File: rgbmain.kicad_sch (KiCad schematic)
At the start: 14 parts, among them J1 Conn_01x10_Pin, J10 Conn_01x04, J2 Conn_01x10_Pin, J3 Conn_01x09_Pin, J4 Conn_01x09, J5 Conn_01x06_Pin, J6 Conn_01x06, J7 Conn_01x13, J8 Conn_01x13, J9 Conn_01x01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

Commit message: footprints added
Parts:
- J1, J2: footprint (none) -> Connector_Molex:Molex_KK-396_A-41792-0010_1x10_P3.96mm_Horizontal
- J10: footprint (none) -> Connector_PinSocket_2.54mm:PinSocket_1x04_P2.54mm_Vertical
- J3, J4: footprint (none) -> Connector_Molex:Molex_KK-396_A-41792-0009_1x09_P3.96mm_Horizontal
- J5, J6: footprint (none) -> Connector_Molex:Molex_KK-396_A-41792-0006_1x06_P3.96mm_Horizontal
- J7, J8: footprint (none) -> rgbmain:Molex_0039532135
- J9: footprint (none) -> Connector_PinHeader_1.00mm:PinHeader_1x01_P1.00mm_Vertical
- R1, R2: footprint (none) -> Resistor_SMD:R_0805_2012Metric_Pad1.20x1.40mm_HandSolder
- U1: footprint (none) -> rgbmain:ElitePi
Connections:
- net +3V3: now also J10.2 (Pin_2); no longer J10.3 (Pin_3)
- net GND: now also J10.1 (Pin_1); no longer J10.4 (Pin_4)
- net SDA0: now also J10.3 (Pin_3); no longer J10.2 (Pin_2)
- net SLC0: now also J10.4 (Pin_4); no longer J10.1 (Pin_1)
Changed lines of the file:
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@@
+	(wire
+		(pts
+			(xy 102.87 26.67) (xy 118.11 26.67)
+		)
+		(stroke
+			(width 0)
+			(type default)
+		)
+	)
 	(wire
 		(pts
@@
 		(pts
 			(xy 121.92 109.22) (xy 121.92 111.76)
-		)
-		(stroke
-			(width 0)
-			(type default)
-		)
-	)
-	(wire
-		(pts
-			(xy 113.03 26.67) (xy 118.11 26.67)
 		)
 		(stroke
@@
 		)
 	)
+	(label "SDA0"
+		(at 113.03 31.75 180)
+		(effects
+			(font
+				(size 1.27 1.27)
+			)
+			(justify right bottom)
+		)
+	)
 	(label "COL_4"
 		(at 30.48 74.93 180)
@@
 		)
 	)
-	(label "SLC0"
-		(at 113.03 26.67 180)
-		(effects
-			(font
-				(size 1.27 1.27)
-			)
-			(justify right bottom)
-		)
-	)
 	(label "ROW_6"
 		(at 162.56 77.47 0)
@@
 		)
 	)
-	(label "SDA0"
-		(at 113.03 29.21 180)
-		(effects
-			(font
-				(size 1.27 1.27)
-			)
-			(justify right bottom)
-		)
-	)
 	(label "COL_9"
 		(at 246.38 72.39 0)
@@
 		)
 	)
+	(label "SLC0"
+		(at 113.03 34.29 180)
+		(effects
+			(font
+				(size 1.27 1.27)
+			)
+			(justify right bottom)
+		)
+	)
 	(label "DOUT_KEY_3V3"
 		(at 162.56 64.77 0)
@@
 			)
 			(justify right bottom)
+		)
+	)
+	(symbol
+		(lib_id "power:+3V3")
+		(at 113.03 29.21 90)
+		(unit 1)
+		(exclude_from_sim no)
+		(in_bom yes)
+		(on_board yes)
+		(dnp no)
+		(fields_autoplaced yes)
+		(property "Reference" "#PWR07"
+			(at 116.84 29.21 0)
+			(effects
+				(font
+					(size 1.27 1.27)
+				)
+				(hide yes)
+			)
+		)
+		(property "Value" "+3V3"
+			(at 109.22 29.2099 90)
+			(effects
+				(font
+					(size 1.27 1.27)
+				)
+				(justify left)
+			)
+		)
+		(property "Footprint" ""
+			(at 113.03 29.21 0)
+			(effects
+				(font
+					(size 1.27 1.27)
+				)
+				(hide yes)
+			)
+		)
+		(property "Datasheet" ""
+			(at 113.03 29.21 0)
+			(effects
+				(font
+					(size 1.27 1.27)
+				)
+				(hide yes)
+			)
+		)
+		(property "Description" "Power symbol creates a global label with name \"+3V3\""
+			(at 113.03 29.21 0)
+			(effects
+				(font
+					(size 1.27 1.27)
+				)
+				(hide yes)
+			)
+		)
+		(pin "1"
+		)
+		(instances
+			(project ""
+				(path "/24ca604d-a7a4-46c7-a288-45b7cfc45cc9"
+					(reference "#PWR07")
+					(unit 1)
+				)
+			)
 		)
 	)
@@
 			)
 		)
-		(property "Footprint" ""
+		(property "Footprint" "rgbmain:Molex_0039532135"
 			(at 38.1 40.64 0)
 			(effects
@@
 			)
 		)
-		(property "Footprint" ""
+		(property "Footprint" "Connector_Molex:Molex_KK-396_A-41792-0006_1x06_P3.96mm_Horizontal"
 			(at 238.76 72.39 0)
 			(effects
@@
 			)
 		)
-		(property "Footprint" ""
+		(property "Footprint" "Connector_Molex:Molex_KK-396_A-41792-0010_1x10_P3.96mm_Horizontal"
 			(at 161.29 144.78 0)
 			(effects
@@
 			)
 		)
-		(property "Footprint" ""
+		(property "Footprint" "Resistor_SMD:R_0805_2012Metric_Pad1.20x1.40mm_HandSolder"
 			(at 187.452 30.48 90)
 			(effects
@@
 			)
 		)
-		(property "Footprint" ""
+		(property "Footprint" "Connector_Molex:Molex_KK-396_A-41792-0006_1x06_P3.96mm_Horizontal"
 			(at 38.1 72.39 0)
 			(effects
@@
 			)
 		)
-		(property "Footprint" ""
+		(property "Footprint" "Connector_Molex:Molex_KK-396_A-41792-0010_1x10_P3.96mm_Horizontal"
 			(at 127 144.78 0)
 			(effects
@@
 				(path "/24ca604d-a7a4-46c7-a288-45b7cfc45cc9"
 					(reference "J1")
+					(unit 1)
+				)
+			)
+		)
+	)
+	(symbol
+		(lib_id "power:GND")
+		(at 102.87 26.67 0)
+		(unit 1)
+		(exclude_from_sim no)
+		(in_bom yes)
+		(on_board yes)
+		(dnp no)
+		(fields_autoplaced yes)
+		(property "Reference" "#PWR06"
+			(at 102.87 33.02 0)
+			(effects
+				(font
+					(size 1.27 1.27)
+				)
+				(hide yes)
+			)
+		)
+		(property "Value" "GND"
+			(at 102.87 31.75 0)
+			(effects
+				(font
+					(size 1.27 1.27)
+				)
+			)
+		)
+		(property "Footprint" ""
+			(at 102.87 26.67 0)
+			(effects
+				(font
+					(size 1.27 1.27)
+				)
+				(hide yes)
+			)
+		)
+		(property "Datasheet" ""
+			(at 102.87 26.67 0)
+			(effects
+				(font
+					(size 1.27 1.27)
+				)
+				(hide yes)
+			)
+		)
+		(property "Description" "Power symbol creates a global label with name \"GND\" , ground"
+			(at 102.87 26.67 0)
+			(effects
+				(font
+					(size 1.27 1.27)
+				)
+				(hide yes)
+			)
+		)
+		(pin "1"
+		)
+		(instances
+			(project ""
+				(path "/24ca604d-a7a4-46c7-a288-45b7cfc45cc9"
+					(reference "#PWR06")
 					(unit 1)
 				)
@@
 			)
 		)
-		(property "Footprint" ""
+		(property "Footprint" "Resistor_SMD:R_0805_2012Metric_Pad1.20x1.40mm_HandSolder"
 			(at 200.152 30.48 90)
 			(effects
@@
 	)
 	(symbol
-		(lib_id "power:+3V3")
-		(at 113.03 31.75 90)
-		(unit 1)
-		(exclude_from_sim no)
-		(in_bom yes)
-		(on_board yes)
-		(dnp no)
-		(fields_autoplaced yes)
-		(property "Reference" "#PWR07"
-			(at 116.84 31.75 0)
-			(effects
-				(font
-					(size 1.27 1.27)
-				)
-				(hide yes)
-			)
-		)
-		(property "Value" "+3V3"
-			(at 109.22 31.7499 90)
-			(effects
-				(font
-					(size 1.27 1.27)
-				)
-				(justify left)
-			)
-		)
-		(property "Footprint" ""
-			(at 113.03 31.75 0)
-			(effects
-				(font
-					(size 1.27 1.27)
-				)
-				(hide yes)
-			)
-		)
-		(property "Datasheet" ""
-			(at 113.03 31.75 0)
-			(effects
-				(font
-					(size 1.27 1.27)
-				)
-				(hide yes)
-			)
-		)
-		(property "Description" "Power symbol creates a global label with name \"+3V3\""
-			(at 113.03 31.75 0)
-			(effects
-				(font
-					(size 1.27 1.27)
-				)
-				(hide yes)
-			)
-		)
-		(pin "1"
-		)
-		(instances
-			(project ""
-				(path "/24ca604d-a7a4-46c7-a288-45b7cfc45cc9"
-					(reference "#PWR07")
-					(unit 1)
-				)
-			)
-		)
-	)
-	(symbol
 		(lib_id "Connector_Generic:Conn_01x01")
 		(at 129.54 104.14 0)
@@
 			)
 		)
-		(property "Footprint" ""
+		(property "Footprint" "Connector_PinHeader_1.00mm:PinHeader_1x01_P1.00mm_Vertical"
 			(at 129.54 104.14 0)
 			(effects
@@
 			)
 		)
-		(property "Footprint" ""
+		(property "Footprint" "rgbmain:ElitePi"
 			(at 144.78 62.23 0)
 			(effects
@@
 			)
 		)
-		(property "Footprint" ""
+		(property "Footprint" "Connector_Molex:Molex_KK-396_A-41792-0009_1x09_P3.96mm_Horizontal"
 			(at 238.76 105.41 0)
 			(effects
@@
 			)
 		)
-		(property "Footprint" ""
+		(property "Footprint" "Connector_Molex:Molex_KK-396_A-41792-0009_1x09_P3.96mm_Horizontal"
 			(at 38.1 105.41 0)
 			(effects
@@
 			)
 		)
-		(property "Footprint" ""
+		(property "Footprint" "Connector_PinSocket_2.54mm:PinSocket_1x04_P2.54mm_Vertical"
 			(at 123.19 29.21 0)
 			(effects
@@
 			)
 		)
-		(property "Footprint" ""
+		(property "Footprint" "rgbmain:Molex_0039532135"
 			(at 238.76 40.64 0)
 			(effects
@@
 					(unit 1)
 				)
-			)
-		)
-	)
-	(symbol
-		(lib_id "power:GND")
-		(at 113.03 34.29 0)
-		(unit 1)
-		(exclude_from_sim no)
-		(in_bom yes)
-		(on_board yes)
-		(dnp no)
-		(fields_autoplaced yes)
-		(property "Reference" "#PWR06"
-			(at 113.03 40.64 0)
-			(effects
-				(font
-					(size 1.27 1.27)
-				)
-				(hide yes)
-			)
-		)
-		(property "Value" "GND"
-			(at 113.03 39.37 0)
-			(effects
-				(font
-					(size 1.27 1.27)
-				)
-			)
-		)
-		(property "Footprint" ""
-			(at 113.03 34.29 0)
-			(effects
-				(font
-					(size 1.27 1.27)
-				)
-				(hide yes)
-			)
-		)
-		(property "Datasheet" ""
-			(at 113.03 34.29 0)
-			(effects
-				(font
-					(size 1.27 1.27)
-				)
-				(hide yes)
-			)
-		)
-		(property "Description" "Power symbol creates a global label with name \"GND\" , ground"
-			(at 113.03 34.29 0)
-			(effects
-				(font
-					(size 1.27 1.27)
-				)
-				(hide yes)
-			)
-		)
-		(pin "1"
-		)
-		(instances
-			(project ""
-				(path "/24ca604d-a7a4-46c7-a288-45b7cfc45cc9"
-					(reference "#PWR06")
-					(unit 1)
-				)

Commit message: use the Molex KK *2.54*
footprints sourced from: https://github.com/SnowMB/pcb_library
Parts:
- added H1: mounting pad, MountingHole:MountingHole_4.3mm_M4_Pad, symbol Mechanical:MountingHole_Pad
- J1, J2: footprint Connector_Molex:Molex_KK-396_A-41792-0010_1x10_P3.96mm_Horizontal -> rgbmain:Molex_KK-254_1x10_P2.54mm_Horizontal
- J3, J4: footprint Connector_Molex:Molex_KK-396_A-41792-0009_1x09_P3.96mm_Horizontal -> rgbmain:Molex_KK-254_1x09_P2.54mm_Horizontal
- J5, J6: footprint Connector_Molex:Molex_KK-396_A-41792-0006_1x06_P3.96mm_Horizontal -> rgbmain:Molex_KK-254_1x06_P2.54mm_Horizontal
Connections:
- net GND: now also H1.1
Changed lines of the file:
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@@
+	(wire
+		(pts
+			(xy 78.74 87.63) (xy 78.74 85.09)
+		)
+		(stroke
+			(width 0)
+			(type default)
+		)
+	)
 	(wire
 		(pts
@@
 		(pts
 			(xy 113.03 29.21) (xy 118.11 29.21)
+		)
+		(stroke
+			(width 0)
+			(type default)
+		)
+	)
+	(wire
+		(pts
+			(xy 78.74 85.09) (xy 88.9 85.09)
 		)
 		(stroke
@@
 				(path "/24ca604d-a7a4-46c7-a288-45b7cfc45cc9"
 					(reference "J7")
+					(unit 1)
+				)
+			)
+		)
+	)
+	(symbol
+		(lib_id "Mechanical:MountingHole_Pad")
+		(at 91.44 85.09 270)
+		(unit 1)
+		(exclude_from_sim no)
+		(in_bom yes)
+		(on_board yes)
+		(dnp no)
+		(property "Reference" "H1"
+			(at 92.0242 87.884 0)
+			(effects
+				(font
+					(size 1.4986 1.4986)
+				)
+				(justify left bottom)
+				(hide yes)
+			)
+		)
+		(property "Value" "mounting pad"
+			(at 83.82 88.9 90)
+			(effects
+				(font
+					(size 1.4986 1.4986)
+				)
+				(justify left bottom)
+			)
+		)
+		(property "Footprint" "MountingHole:MountingHole_4.3mm_M4_Pad"
+			(at 91.44 85.09 0)
+			(effects
+				(font
+					(size 1.27 1.27)
+				)
+				(hide yes)
+			)
+		)
+		(property "Datasheet" ""
+			(at 91.44 85.09 0)
+			(effects
+				(font
+					(size 1.27 1.27)
+				)
+				(hide yes)
+			)
+		)
+		(property "Description" ""
+			(at 91.44 85.09 0)
+			(effects
+				(font
+					(size 1.27 1.27)
+				)
+			)
+		)
+		(pin "1"
+		)
+		(instances
+			(project "rgbmain"
+				(path "/24ca604d-a7a4-46c7-a288-45b7cfc45cc9"
+					(reference "H1")
 					(unit 1)
 				)
@@
 			)
 		)
-		(property "Footprint" "Connector_Molex:Molex_KK-396_A-41792-0006_1x06_P3.96mm_Horizontal"
+		(property "Footprint" "rgbmain:Molex_KK-254_1x06_P2.54mm_Horizontal"
 			(at 238.76 72.39 0)
 			(effects
@@
 			)
 		)
-		(property "Footprint" "Connector_Molex:Molex_KK-396_A-41792-0010_1x10_P3.96mm_Horizontal"
+		(property "Footprint" "rgbmain:Molex_KK-254_1x10_P2.54mm_Horizontal"
 			(at 161.29 144.78 0)
 			(effects
@@
 			)
 		)
-		(property "Footprint" "Connector_Molex:Molex_KK-396_A-41792-0006_1x06_P3.96mm_Horizontal"
+		(property "Footprint" "rgbmain:Molex_KK-254_1x06_P2.54mm_Horizontal"
 			(at 38.1 72.39 0)
 			(effects
@@
 			)
 		)
-		(property "Footprint" "Connector_Molex:Molex_KK-396_A-41792-0010_1x10_P3.96mm_Horizontal"
+		(property "Footprint" "rgbmain:Molex_KK-254_1x10_P2.54mm_Horizontal"
 			(at 127 144.78 0)
 			(effects
@@
 			)
 		)
-		(property "Footprint" "Connector_Molex:Molex_KK-396_A-41792-0009_1x09_P3.96mm_Horizontal"
+		(property "Footprint" "rgbmain:Molex_KK-254_1x09_P2.54mm_Horizontal"
 			(at 238.76 105.41 0)
 			(effects
@@
 			)
 		)
-		(property "Footprint" "Connector_Molex:Molex_KK-396_A-41792-0009_1x09_P3.96mm_Horizontal"
+		(property "Footprint" "rgbmain:Molex_KK-254_1x09_P2.54mm_Horizontal"
 			(at 38.1 105.41 0)
 			(effects
@@
 					(unit 1)
 				)
+			)
+		)
+	)
+	(symbol
+		(lib_id "power:GND")
+		(at 78.74 87.63 0)
+		(unit 1)
+		(exclude_from_sim no)
+		(in_bom yes)
+		(on_board yes)
+		(dnp no)
+		(fields_autoplaced yes)
+		(property "Reference" "#PWR08"
+			(at 78.74 93.98 0)
+			(effects
+				(font
+					(size 1.27 1.27)
+				)
+				(hide yes)
+			)
+		)
+		(property "Value" "GND"
+			(at 78.74 92.71 0)
+			(effects
+				(font
+					(size 1.27 1.27)
+				)
+			)
+		)
+		(property "Footprint" ""
+			(at 78.74 87.63 0)
+			(effects
+				(font
+					(size 1.27 1.27)
+				)
+				(hide yes)
+			)
+		)
+		(property "Datasheet" ""
+			(at 78.74 87.63 0)
+			(effects
+				(font
+					(size 1.27 1.27)
+				)
+				(hide yes)
+			)
+		)
+		(property "Description" "Power symbol creates a global label with name \"GND\" , ground"
+			(at 78.74 87.63 0)
+			(effects
+				(font
+					(size 1.27 1.27)
+				)
+				(hide yes)
+			)
+		)
+		(pin "1"
+		)
+		(instances
+			(project ""
+				(path "/24ca604d-a7a4-46c7-a288-45b7cfc45cc9"
+					(reference "#PWR08")
+					(unit 1)
+				)

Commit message: use vertical pcb connectors
horizontal take up too much board space
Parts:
- J1, J2: footprint rgbmain:Molex_KK-254_1x10_P2.54mm_Horizontal -> Connector_Molex:Molex_KK-254_AE-6410-10A_1x10_P2.54mm_Vertical
- J3, J4: footprint rgbmain:Molex_KK-254_1x09_P2.54mm_Horizontal -> Connector_Molex:Molex_KK-254_AE-6410-09A_1x09_P2.54mm_Vertical
- J5, J6: footprint rgbmain:Molex_KK-254_1x06_P2.54mm_Horizontal -> Connector_Molex:Molex_KK-254_AE-6410-06A_1x06_P2.54mm_Vertical
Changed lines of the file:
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@@
 			)
 		)
-		(property "Footprint" "rgbmain:Molex_KK-254_1x06_P2.54mm_Horizontal"
+		(property "Footprint" "Connector_Molex:Molex_KK-254_AE-6410-06A_1x06_P2.54mm_Vertical"
 			(at 238.76 72.39 0)
 			(effects
@@
 			)
 		)
-		(property "Footprint" "rgbmain:Molex_KK-254_1x10_P2.54mm_Horizontal"
+		(property "Footprint" "Connector_Molex:Molex_KK-254_AE-6410-10A_1x10_P2.54mm_Vertical"
 			(at 161.29 144.78 0)
 			(effects
@@
 			)
 		)
-		(property "Footprint" "rgbmain:Molex_KK-254_1x06_P2.54mm_Horizontal"
+		(property "Footprint" "Connector_Molex:Molex_KK-254_AE-6410-06A_1x06_P2.54mm_Vertical"
 			(at 38.1 72.39 0)
 			(effects
@@
 			)
 		)
-		(property "Footprint" "rgbmain:Molex_KK-254_1x10_P2.54mm_Horizontal"
+		(property "Footprint" "Connector_Molex:Molex_KK-254_AE-6410-10A_1x10_P2.54mm_Vertical"
 			(at 127 144.78 0)
 			(effects
@@
 			)
 		)
-		(property "Footprint" "rgbmain:Molex_KK-254_1x09_P2.54mm_Horizontal"
+		(property "Footprint" "Connector_Molex:Molex_KK-254_AE-6410-09A_1x09_P2.54mm_Vertical"
 			(at 238.76 105.41 0)
 			(effects
@@
 			)
 		)
-		(property "Footprint" "rgbmain:Molex_KK-254_1x09_P2.54mm_Horizontal"
+		(property "Footprint" "Connector_Molex:Molex_KK-254_AE-6410-09A_1x09_P2.54mm_Vertical"
 			(at 38.1 105.41 0)
 			(effects

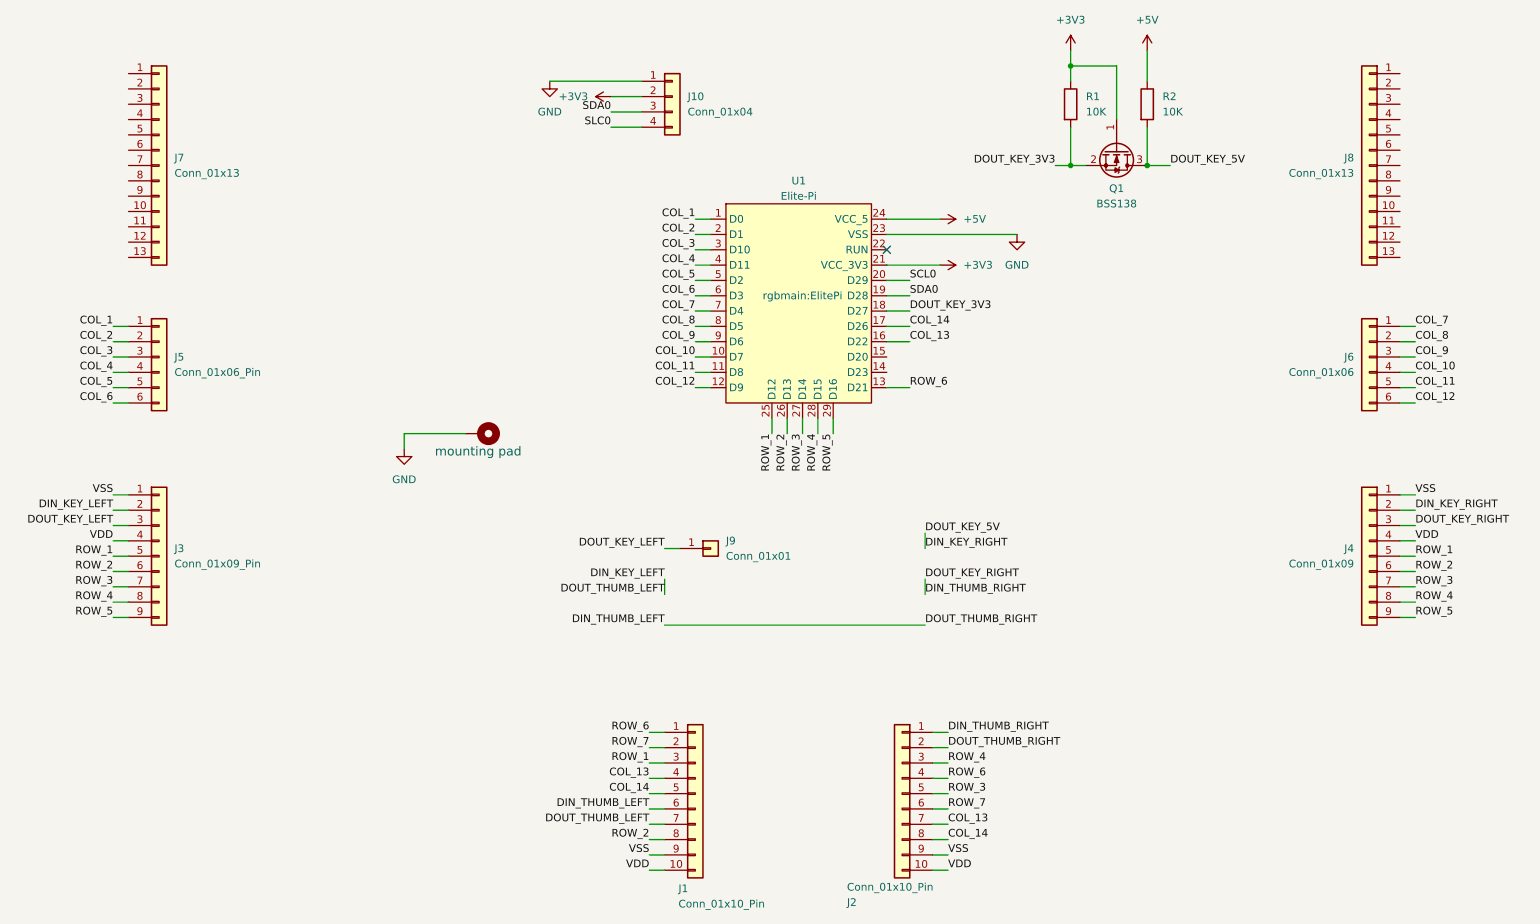
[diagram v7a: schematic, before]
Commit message: wired up all function keys
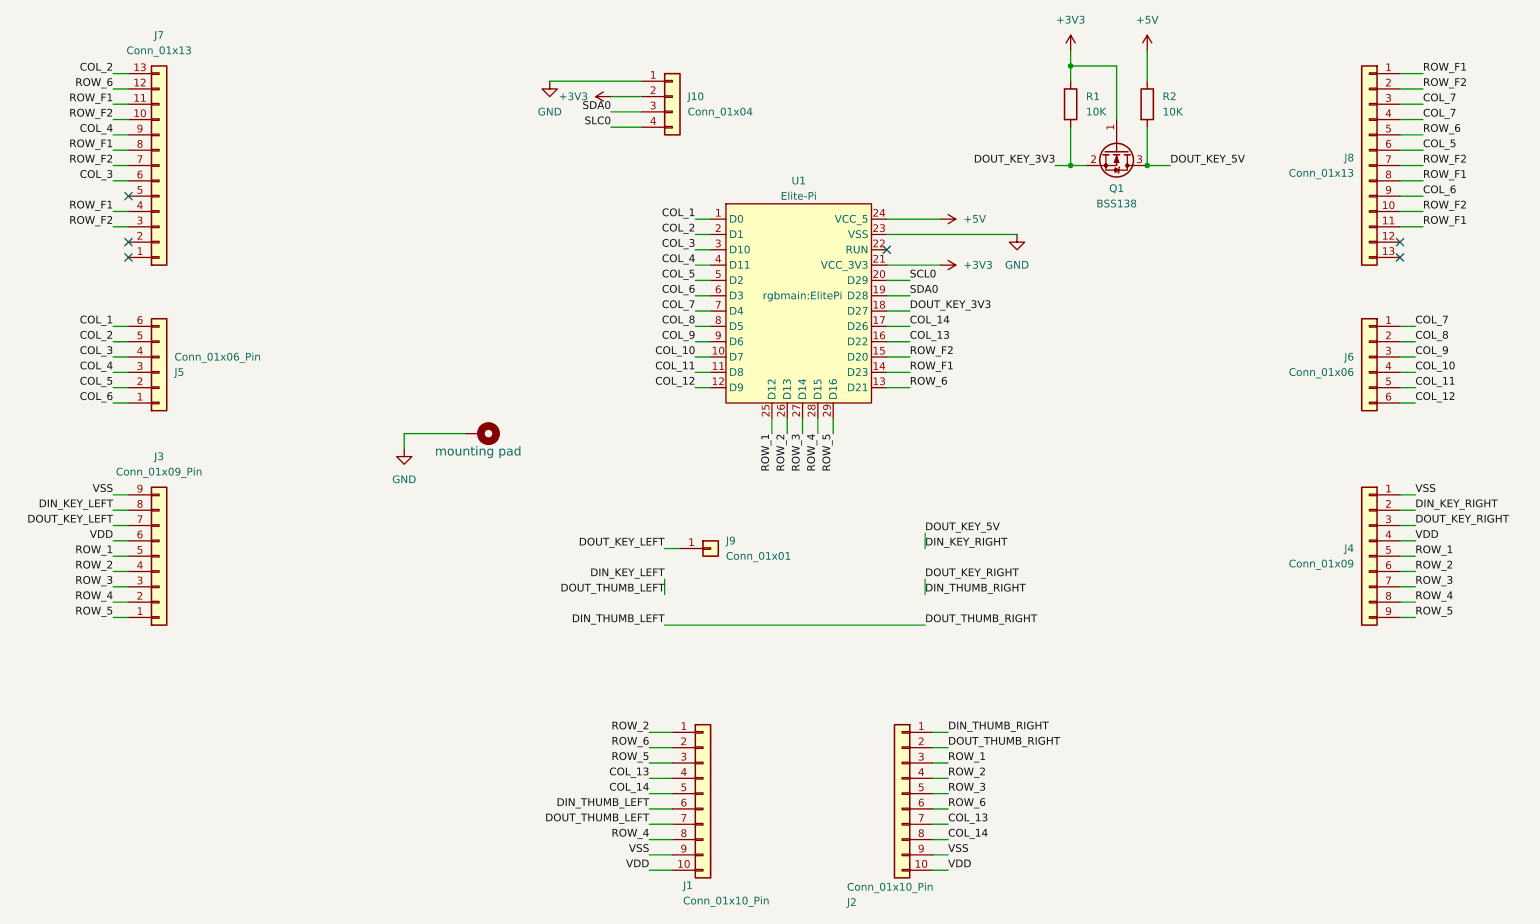
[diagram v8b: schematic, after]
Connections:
- net ROW_7 is gone; now on net ROW_6: J1.2 (Pin_2), J2.6 (Pin_6)
- net COL_1: now also J5.6 (Pin_6); no longer J5.1 (Pin_1)
- net COL_2: now also J5.5 (Pin_5), J7.13 (Pin_13); no longer J5.2 (Pin_2)
- net COL_3: now also J5.4 (Pin_4), J7.6 (Pin_6); no longer J5.3 (Pin_3)
- net COL_4: now also J5.3 (Pin_3), J7.9 (Pin_9); no longer J5.4 (Pin_4)
- net COL_5: now also J5.2 (Pin_2), J8.6 (Pin_6); no longer J5.5 (Pin_5)
- net COL_6: now also J5.1 (Pin_1), J8.9 (Pin_9); no longer J5.6 (Pin_6)
- net COL_7: now also J8.3 (Pin_3), J8.4 (Pin_4)
- net DIN_KEY_LEFT: now also J3.8 (Pin_8); no longer J3.2 (Pin_2)
- net DOUT_KEY_LEFT: now also J3.7 (Pin_7); no longer J3.3 (Pin_3)
- net ROW_1: now also J2.3 (Pin_3); no longer J1.3 (Pin_3)
- net ROW_2: now also J1.1 (Pin_1), J2.4 (Pin_4), J3.4 (Pin_4); no longer J1.8 (Pin_8), J3.6 (Pin_6)
- net ROW_3: now also J3.3 (Pin_3); no longer J3.7 (Pin_7)
- net ROW_4: now also J1.8 (Pin_8), J3.2 (Pin_2); no longer J2.3 (Pin_3), J3.8 (Pin_8)
- net ROW_5: now also J1.3 (Pin_3), J3.1 (Pin_1); no longer J3.9 (Pin_9)
- net ROW_6: now also J7.12 (Pin_12), J8.5 (Pin_5); no longer J1.1 (Pin_1), J2.4 (Pin_4)
- net VDD: now also J3.6 (Pin_6); no longer J3.4 (Pin_4)
- net VSS: now also J3.9 (Pin_9); no longer J3.1 (Pin_1)
- net ROW_F2: now reaches J7.10 (Pin_10)
- net ROW_F2: now also J7.3 (Pin_3), J7.7 (Pin_7), J8.10 (Pin_10), J8.2 (Pin_2), J8.7 (Pin_7), U1.15 (D20)
- net ROW_F1: now reaches J7.11 (Pin_11)
- net ROW_F1: now also J7.4 (Pin_4), J7.8 (Pin_8), J8.1 (Pin_1), J8.11 (Pin_11), J8.8 (Pin_8), U1.14 (D23)
- no-connect marks 1 -> 6
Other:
- moved on the sheet: J1
